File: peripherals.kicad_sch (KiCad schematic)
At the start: 67 parts, among them J1 ERF8-040-05.0-L-DV-K-TR, J801 TC2050-IDC-NL, J803 533980471, Q801 BSS138W-7-F, Q802 BSS138W-7-F, Q803 BSS138W-7-F, Q804 BSS138W-7-F, U803 PCAL6416AHF, U805 AP22615, U806 AP22615, U807 74LVC1T45GM

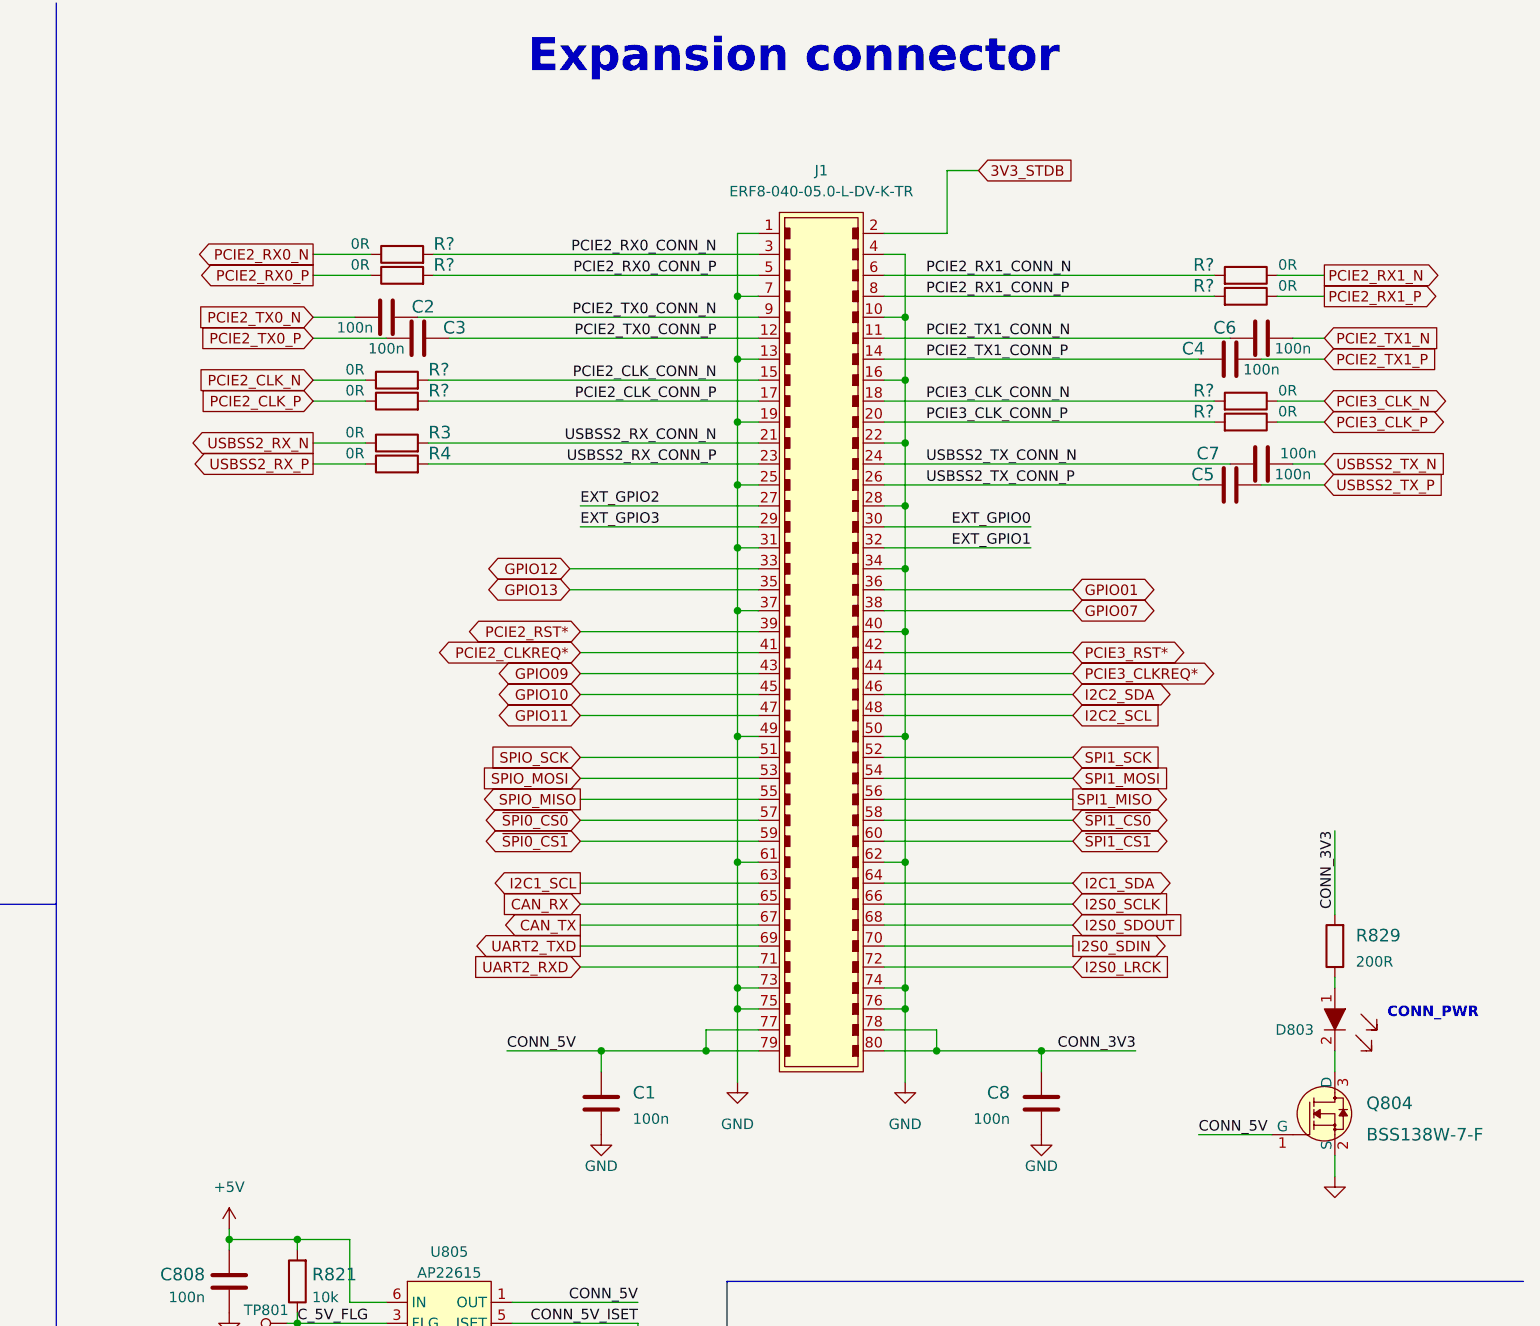
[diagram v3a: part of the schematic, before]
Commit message: Use 1uF caps on power going to expansion connector
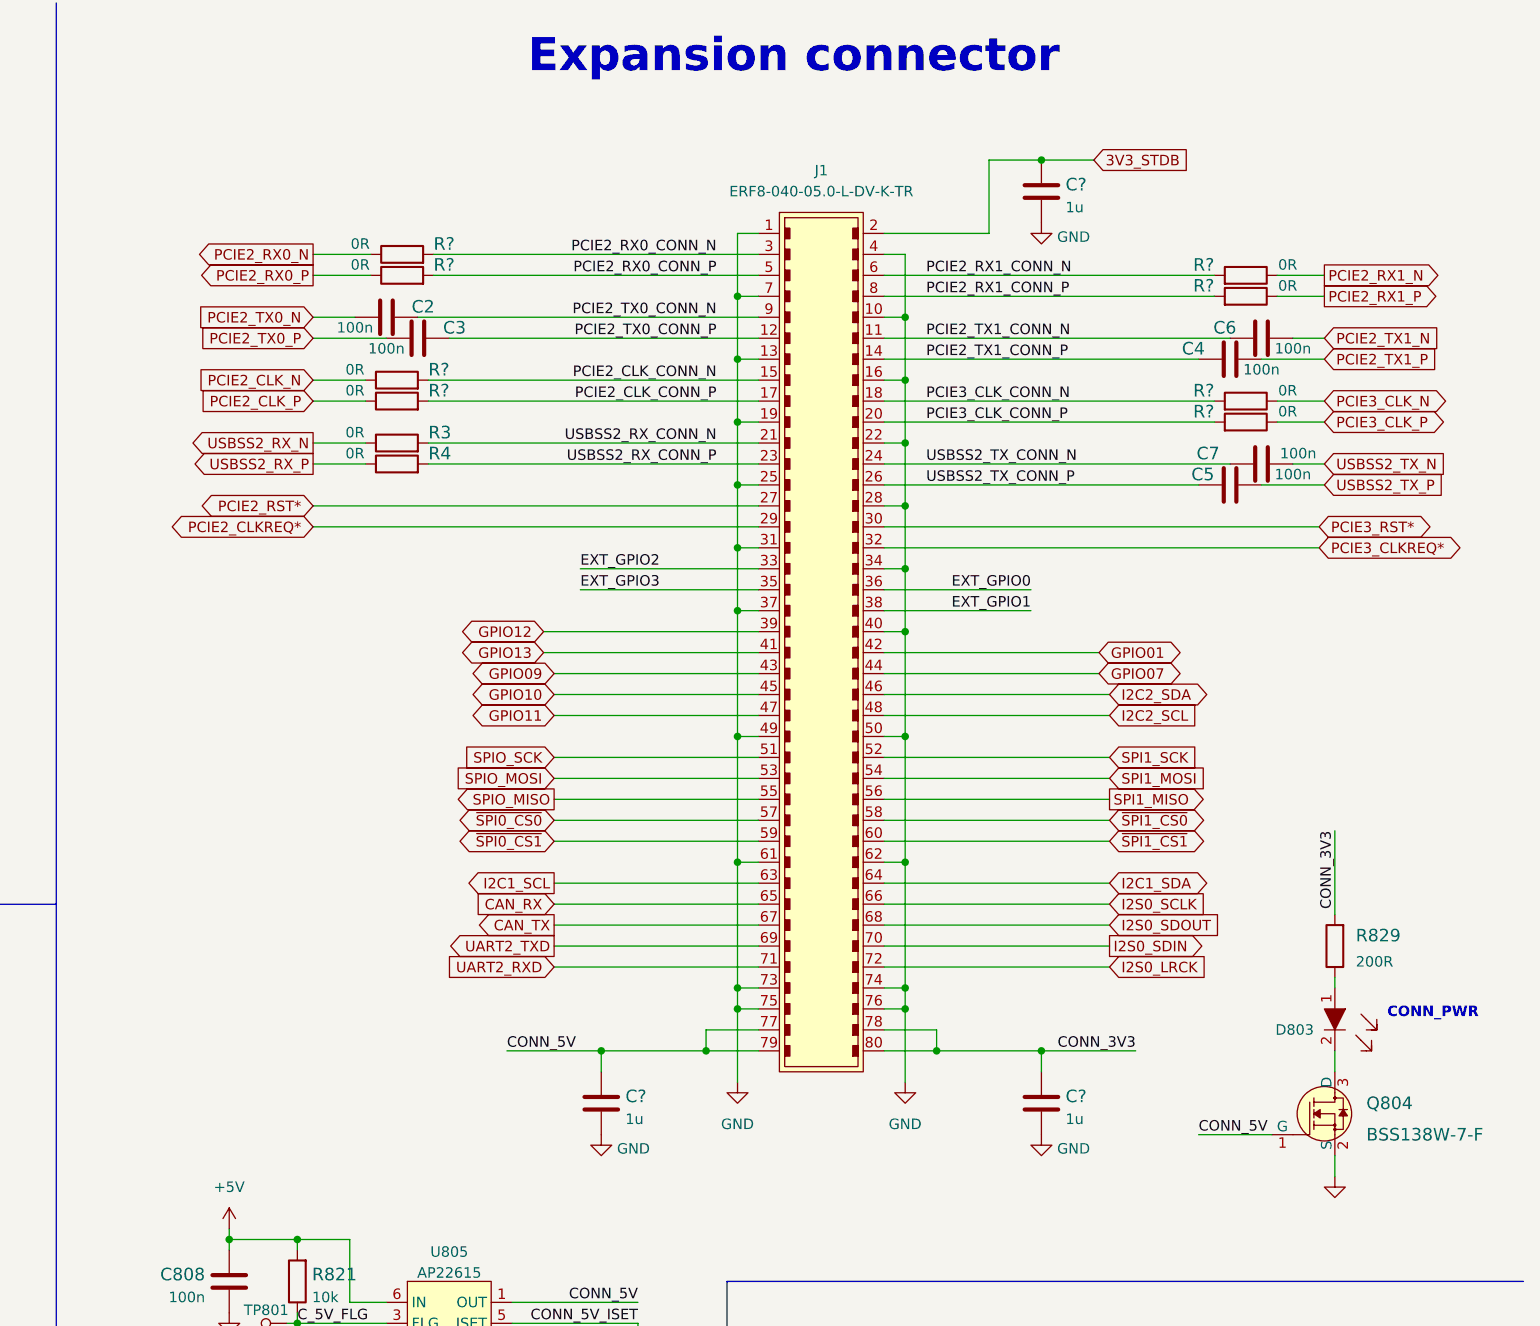
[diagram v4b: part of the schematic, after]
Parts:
- removed C1, C8: C_100n_0402, antmicro-footprints:0402-cap, symbol antmicroCapacitors0402:C_100n_0402
- added C? (x3): C_1u_0402, antmicro-footprints:0402-cap, symbol antmicroCapacitors0402:C_1u_0402
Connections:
- net 3V3_STDB: now also C?.1
- net CONN_3V3: now also C?.1
- net CONN_5V: now also C?.1
- net EXT_GPIO0: now also J1.36; no longer J1.30
- net EXT_GPIO1: now also J1.38; no longer J1.32
- net EXT_GPIO2: now also J1.33; no longer J1.27
- net EXT_GPIO3: now also J1.35; no longer J1.29
- net GND: now also C?.2, C?.2, C?.2
- net GPIO01: now also J1.42; no longer J1.36
- net GPIO07: now also J1.44; no longer J1.38
- net GPIO12: now also J1.39; no longer J1.33
- net GPIO13: now also J1.41; no longer J1.35
- net PCIE2_CLKREQ*: now also J1.29; no longer J1.41
- net PCIE2_RST*: now also J1.27; no longer J1.39
- net PCIE3_CLKREQ*: now also J1.32; no longer J1.44
- net PCIE3_RST*: now also J1.30; no longer J1.42

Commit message: Component annotation
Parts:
- gave numbers to parts that had none: 11
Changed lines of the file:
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@@
   (symbol (lib_id "power:GND") (at 295.91 149.86 0) (unit 1)
     (in_bom yes) (on_board yes) (fields_autoplaced)
-    (property "Reference" "#PWR?" (id 0) (at 295.91 156.21 0)
+    (property "Reference" "#PWR0162" (id 0) (at 295.91 156.21 0)
       (effects (font (size 1.27 1.27)) hide)
     )
@@
   (symbol (lib_id "antmicroResistors0402:R_0R_0402") (at 374.015 48.26 0) (mirror y) (unit 1)
     (in_bom yes) (on_board yes)
-    (property "Reference" "R?" (id 0) (at 370.205 46.99 0)
+    (property "Reference" "R10" (id 0) (at 370.205 46.99 0)
       (effects (font (size 1.524 1.524)) (justify left))
     )
@@
   (symbol (lib_id "power:GND") (at 349.25 39.37 0) (unit 1)
     (in_bom yes) (on_board yes) (fields_autoplaced)
-    (property "Reference" "#PWR?" (id 0) (at 349.25 45.72 0)
+    (property "Reference" "#PWR0159" (id 0) (at 349.25 45.72 0)
       (effects (font (size 1.27 1.27)) hide)
     )
@@
   (symbol (lib_id "antmicroCapacitors0402:C_1u_0402") (at 295.91 146.05 0) (unit 1)
     (in_bom yes) (on_board yes) (fields_autoplaced)
-    (property "Reference" "C?" (id 0) (at 298.831 145.2154 0)
+    (property "Reference" "C1" (id 0) (at 298.831 145.2154 0)
       (effects (font (size 1.524 1.524)) (justify left))
     )
@@
   (symbol (lib_id "antmicroResistors0402:R_0R_0402") (at 374.015 60.96 0) (mirror y) (unit 1)
     (in_bom yes) (on_board yes)
-    (property "Reference" "R?" (id 0) (at 370.205 59.69 0)
+    (property "Reference" "R11" (id 0) (at 370.205 59.69 0)
       (effects (font (size 1.524 1.524)) (justify left))
     )
@@
   (symbol (lib_id "antmicroResistors0402:R_0R_0402") (at 271.145 60.96 0) (unit 1)
     (in_bom yes) (on_board yes)
-    (property "Reference" "R?" (id 0) (at 274.955 59.69 0)
+    (property "Reference" "R6" (id 0) (at 274.955 59.69 0)
       (effects (font (size 1.524 1.524)) (justify left))
     )
@@
   (symbol (lib_id "antmicroResistors0402:R_0R_0402") (at 271.78 43.18 0) (unit 1)
     (in_bom yes) (on_board yes)
-    (property "Reference" "R?" (id 0) (at 275.59 41.91 0)
+    (property "Reference" "R7" (id 0) (at 275.59 41.91 0)
       (effects (font (size 1.524 1.524)) (justify left))
     )
@@
   (symbol (lib_id "antmicroCapacitors0402:C_1u_0402") (at 349.25 146.05 0) (unit 1)
     (in_bom yes) (on_board yes) (fields_autoplaced)
-    (property "Reference" "C?" (id 0) (at 352.171 145.2154 0)
+    (property "Reference" "C9" (id 0) (at 352.171 145.2154 0)
       (effects (font (size 1.524 1.524)) (justify left))
     )
@@
   (symbol (lib_id "antmicroCapacitors0402:C_1u_0402") (at 349.25 35.56 0) (unit 1)
     (in_bom yes) (on_board yes) (fields_autoplaced)
-    (property "Reference" "C?" (id 0) (at 352.171 34.7254 0)
+    (property "Reference" "C8" (id 0) (at 352.171 34.7254 0)
       (effects (font (size 1.524 1.524)) (justify left))
     )
@@
   (symbol (lib_id "antmicroResistors0402:R_0R_0402") (at 374.015 45.72 0) (mirror y) (unit 1)
     (in_bom yes) (on_board yes)
-    (property "Reference" "R?" (id 0) (at 370.205 44.45 0)
+    (property "Reference" "R9" (id 0) (at 370.205 44.45 0)
       (effects (font (size 1.524 1.524)) (justify left))
     )
@@
   (symbol (lib_id "antmicroResistors0402:R_0R_0402") (at 271.145 58.42 0) (unit 1)
     (in_bom yes) (on_board yes)
-    (property "Reference" "R?" (id 0) (at 274.955 57.15 0)
+    (property "Reference" "R5" (id 0) (at 274.955 57.15 0)
       (effects (font (size 1.524 1.524)) (justify left))
     )
@@
   (symbol (lib_id "power:GND") (at 349.25 149.86 0) (unit 1)
     (in_bom yes) (on_board yes) (fields_autoplaced)
-    (property "Reference" "#PWR?" (id 0) (at 349.25 156.21 0)
+    (property "Reference" "#PWR0163" (id 0) (at 349.25 156.21 0)
       (effects (font (size 1.27 1.27)) hide)
     )
@@
   (symbol (lib_id "antmicroResistors0402:R_0R_0402") (at 271.78 45.72 0) (unit 1)
     (in_bom yes) (on_board yes)
-    (property "Reference" "R?" (id 0) (at 275.59 44.45 0)
+    (property "Reference" "R8" (id 0) (at 275.59 44.45 0)
       (effects (font (size 1.524 1.524)) (justify left))
     )
@@
   (symbol (lib_id "antmicroResistors0402:R_0R_0402") (at 374.015 63.5 0) (mirror y) (unit 1)
     (in_bom yes) (on_board yes)
-    (property "Reference" "R?" (id 0) (at 370.205 62.23 0)
-      (effects (font (size 1.524 1.524)) (justify left))
-    )
+    (property "Reference" "R12" (id 0) (at 370.205 62.23 0)
+      (effects (font (size 1.524 1.524)) (justify left))
+    )

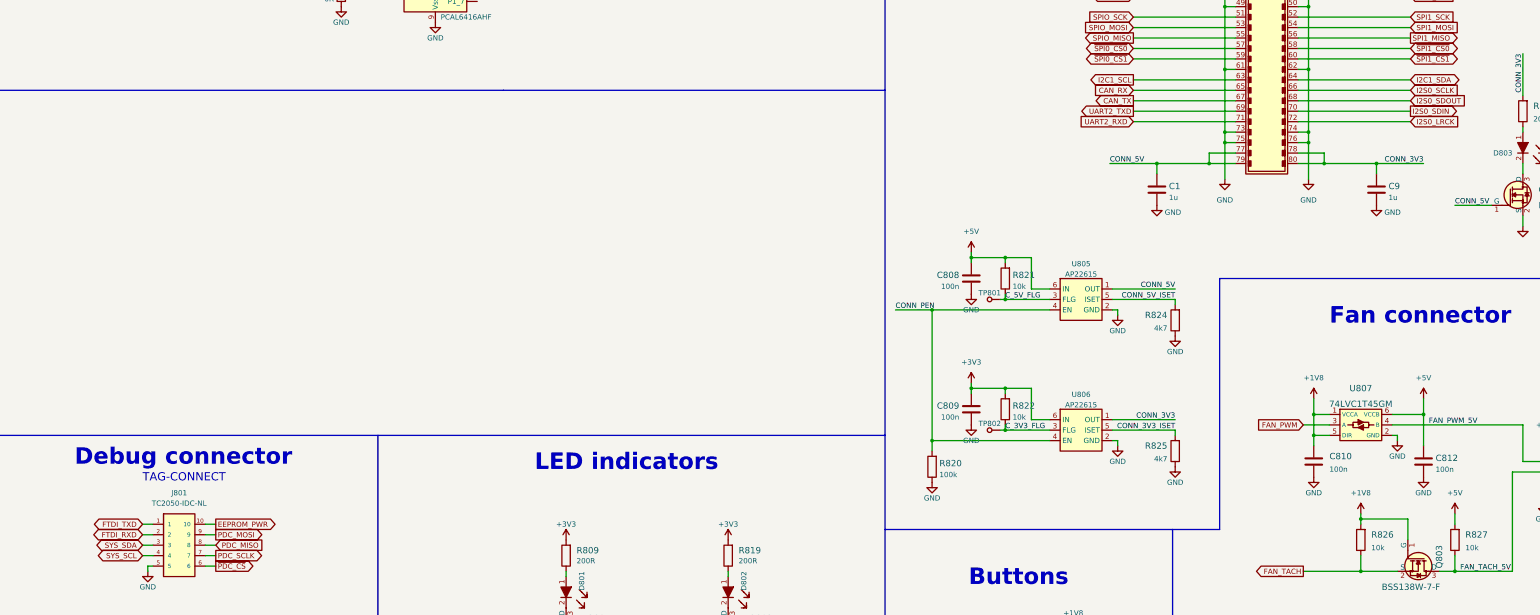
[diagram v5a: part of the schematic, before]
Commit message: Fix UART2 connected to expansion connector, add I2S, UART to M.2
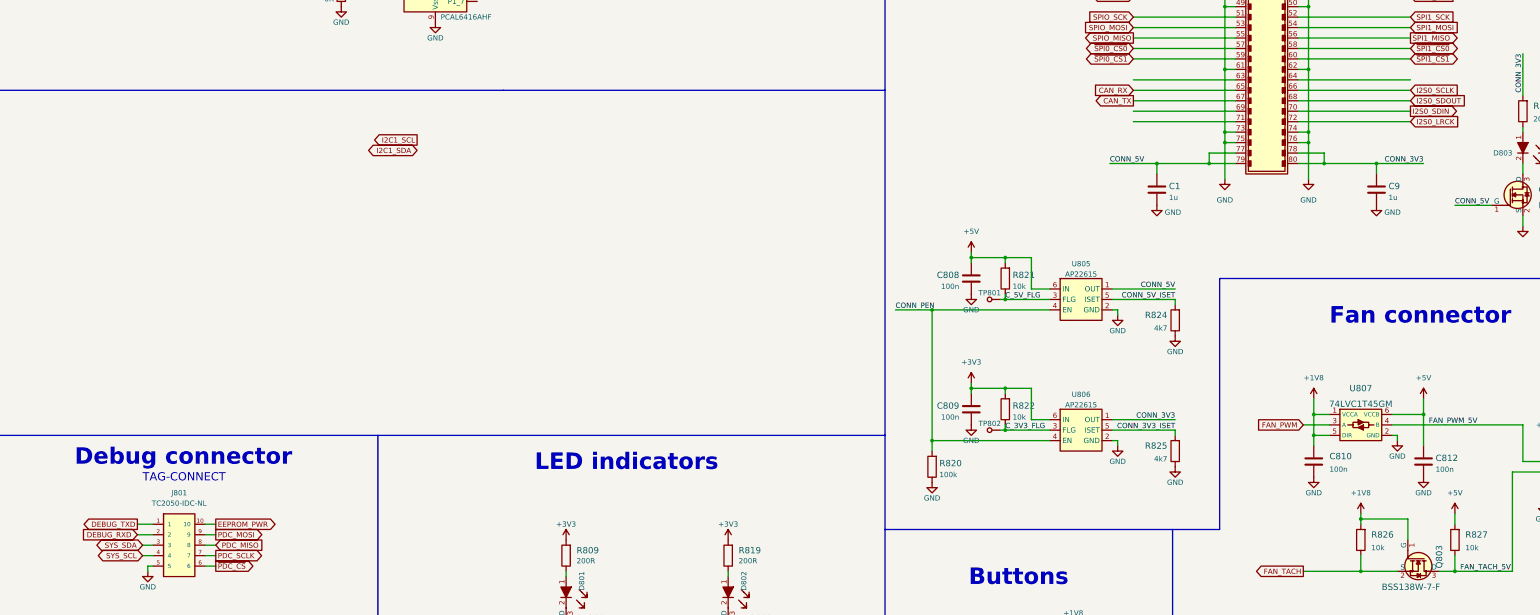
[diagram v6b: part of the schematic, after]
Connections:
- net I2C1_SCL: no longer J1.63
- net I2C1_SDA: no longer J1.64
- net FTDI_RXD renamed DEBUG_RXD
- net FTDI_TXD renamed DEBUG_TXD
- net UART2_RXD: no longer names the net of J1.71
- net UART2_TXD: no longer names the net of J1.69
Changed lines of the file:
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@@
     (stroke (width 0) (type default) (color 0 0 0 0))
   )
-  (wire (pts (xy 49.53 227.33) (xy 52.07 227.33))
+  (wire (pts (xy 48.26 227.33) (xy 52.07 227.33))
     (stroke (width 0) (type default) (color 0 0 0 0))
   )
@@
     (stroke (width 0) (type default) (color 0 0 0 0))
   )
-  (wire (pts (xy 49.53 229.87) (xy 52.07 229.87))
+  (wire (pts (xy 48.26 229.87) (xy 52.07 229.87))
     (stroke (width 0) (type default) (color 0 0 0 0))
   )
@@
     )
   )
-  (global_label "FTDI_RXD" (shape bidirectional) (at 49.53 229.87 180)
+  (global_label "DEBUG_RXD" (shape input) (at 48.26 229.87 180)
     (effects (font (size 1.27 1.27)) (justify right))
-    (property "Intersheet References" "${INTERSHEET_REFS}" (id 0) (at 36.83 229.87 0)
+    (property "Intersheet References" "${INTERSHEET_REFS}" (id 0) (at 34.29 229.87 0)
       (effects (font (size 1.27 1.27)) (justify right))
     )
@@
     )
   )
-  (global_label "FTDI_TXD" (shape bidirectional) (at 49.53 227.33 180)
-    (effects (font (size 1.27 1.27)) (justify right))
-    (property "Intersheet References" "${INTERSHEET_REFS}" (id 0) (at 36.83 227.33 0)
-      (effects (font (size 1.27 1.27)) (justify right))
-    )
-  )
   (global_label "GPIO11" (shape bidirectional) (at 290.195 99.06 180)
     (effects (font (size 1.27 1.27)) (justify right))
@@
     )
   )
-  (global_label "UART2_TXD" (shape output) (at 290.195 127 180)
-    (effects (font (size 1.27 1.27)) (justify right))
-    (property "Intersheet References" "${INTERSHEET_REFS}" (id 0) (at 274.955 127 0)
-      (effects (font (size 1.27 1.27)) (justify right))
-    )
-  )
   (global_label "PCIE2_TX1_P" (shape input) (at 383.54 55.88 0)
     (effects (font (size 1.27 1.27)) (justify left))
@@
     )
   )
-  (global_label "I2C1_SCL" (shape output) (at 290.195 119.38 180)
+  (global_label "DEBUG_TXD" (shape output) (at 48.26 227.33 180)
+    (effects (font (size 1.27 1.27)) (justify right))
+    (property "Intersheet References" "${INTERSHEET_REFS}" (id 0) (at 34.29 227.33 0)
+      (effects (font (size 1.27 1.27)) (justify right))
+    )
+  )
+  (global_label "I2C1_SCL" (shape output) (at 116.205 133.985 180)
     (effects (font (size 1.27 1.27)) (justify right))
-    (property "Intersheet References" "${INTERSHEET_REFS}" (id 0) (at 274.955 119.38 0)
+    (property "Intersheet References" "${INTERSHEET_REFS}" (id 0) (at 100.965 133.985 0)
       (effects (font (size 1.27 1.27)) (justify right))
     )
@@
     )
   )
-  (global_label "UART2_RXD" (shape input) (at 290.195 129.54 180)
-    (effects (font (size 1.27 1.27)) (justify right))
-    (property "Intersheet References" "${INTERSHEET_REFS}" (id 0) (at 274.955 129.54 0)
-      (effects (font (size 1.27 1.27)) (justify right))
-    )
-  )
   (global_label "SPI1_MOSI" (shape input) (at 357.505 106.68 0)
     (effects (font (size 1.27 1.27)) (justify left))
@@
     )
   )
-  (global_label "I2C1_SDA" (shape bidirectional) (at 357.505 119.38 0)
-    (effects (font (size 1.27 1.27)) (justify left))
-    (property "Intersheet References" "${INTERSHEET_REFS}" (id 0) (at 371.475 119.38 0)
-      (effects (font (size 1.27 1.27)) (justify left))
+  (global_label "I2C1_SDA" (shape bidirectional) (at 116.205 136.525 180)
+    (effects (font (size 1.27 1.27)) (justify right))
+    (property "Intersheet References" "${INTERSHEET_REFS}" (id 0) (at 102.235 136.525 0)
+      (effects (font (size 1.27 1.27)) (justify right))
     )
   )

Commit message: Improved connector pinout
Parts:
- removed C8: C_1u_0402, antmicro-footprints:0402-cap, symbol antmicroCapacitors0402:C_1u_0402
- added C?: C_1u_0402, antmicro-footprints:0402-cap, symbol antmicroCapacitors0402:C_1u_0402
- added R?: R_0R_0603, antmicro-footprints:0603-res, symbol antmicroResistors0603:R_0R_0603
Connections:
- net +1V8: now also R?.2
- net 3V3_STDB: now also J1.76, C?.1; no longer J1.2
- net EXT_GPIO0: now also J1.31; no longer J1.36
- net EXT_GPIO1: now also J1.33; no longer J1.38
- net EXT_GPIO2: now also J1.35; no longer J1.33
- net EXT_GPIO3: now also J1.36; no longer J1.35
- net EXT_GPIO4: now also J1.40
- net GND: now also J1.2, J1.38, C?.2; no longer J1.31, J1.34, J1.40, J1.73, J1.76
- net GPIO01: now also J1.39; no longer J1.42
- net GPIO07: now also J1.41; no longer J1.44
- net GPIO12: now also J1.42; no longer J1.39
- net GPIO13: now also J1.44; no longer J1.41
- net SYS_SCL: now also J1.64
- net SYS_SDA: now also J1.63
- net UART0_TXD: now reaches J1.69
- net UART0_RXD: now reaches J1.71
- new net: J1.73, R?.1
- new net PCIE_WAKE_EXT: J1.34
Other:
- note added: "LOW POWER ONLY FOR LEVEL SHIFTERS"
- moved on the sheet: C1, C2, C3, C4, C5, C6, C7, C804, C9, D803, J1, Q804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
